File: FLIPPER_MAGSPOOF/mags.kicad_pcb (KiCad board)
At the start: 2 copper layers, 67 x 34 mm, 5 parts, among them J1 Coil, J2 Conn_01x10_Socket, J3 Conn_01x08_Socket, U1 TC4424

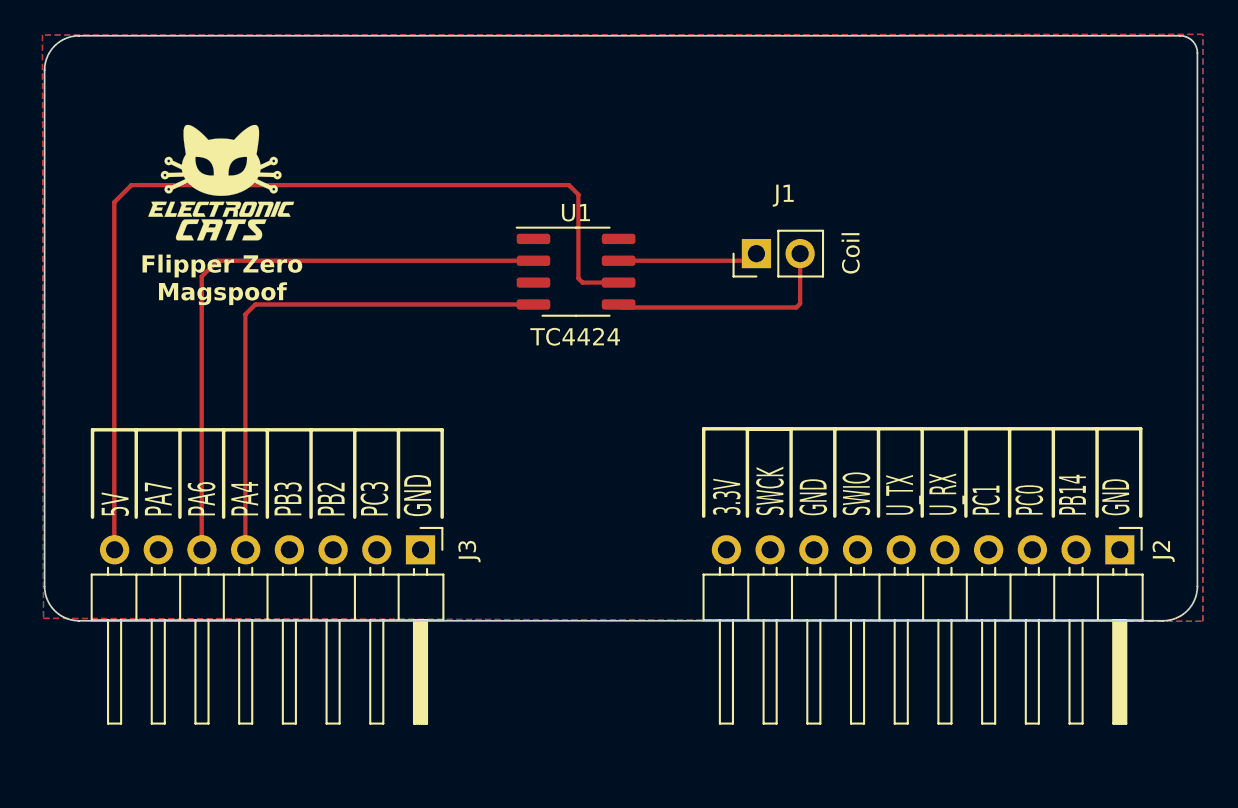
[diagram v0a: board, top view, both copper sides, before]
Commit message: add BOM and serigraphy
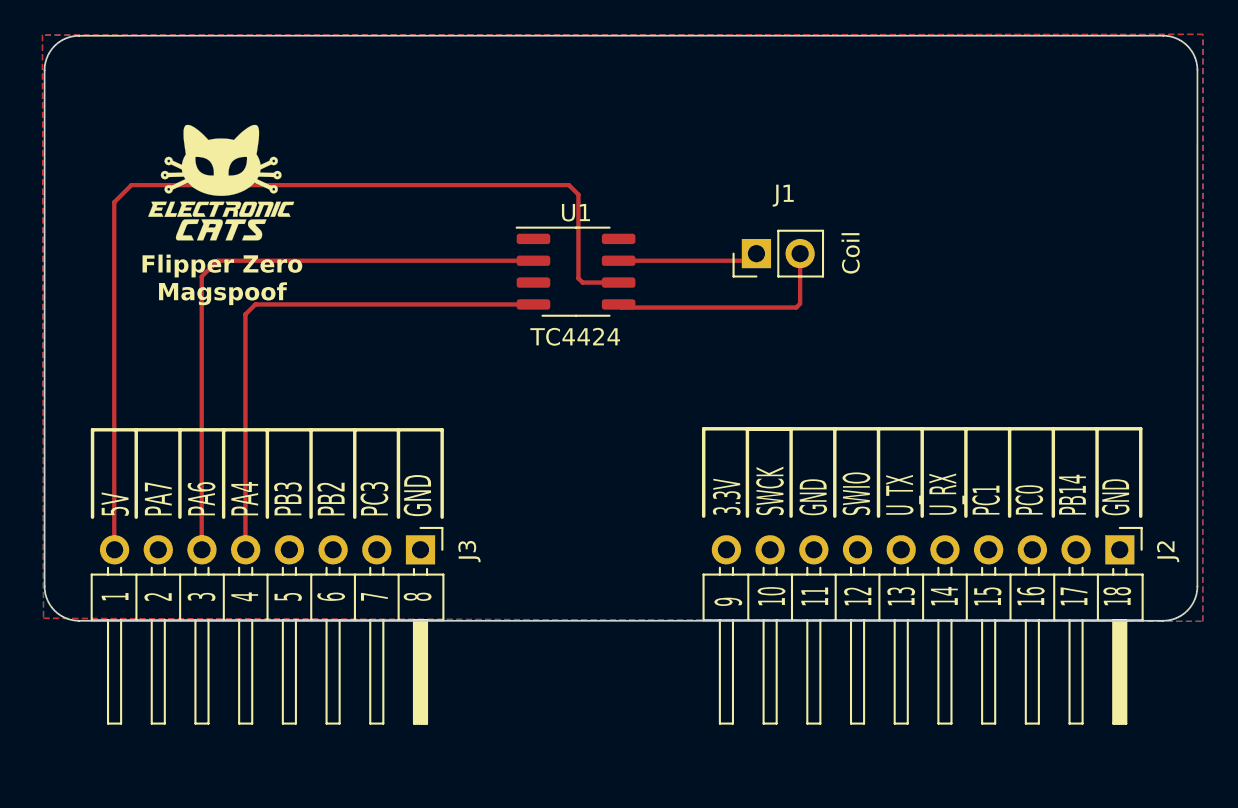
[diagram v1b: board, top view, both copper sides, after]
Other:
- outline, holes or cut-outs redrawn
- board text added: "1 2 3 4 5 6 7 8"
- board text added: "9 10 11 12 13 14 15 16 17 18"
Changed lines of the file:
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@@
         (effects (font (size 1 1) (thickness 0.15)))
     )
-    (fp_text user "${REFERENCE}" (at 2.77 8.89) (layer "F.Fab")
-        (effects (font (size 1 1) (thickness 0.15)))
-    )
     (fp_line (start -1.27 -1.27) (end 0 -1.27)
       (stroke (width 0.12) (type solid)) (layer "F.SilkS"))
@@
       (net 8 "+5V") (pinfunction "Pin_1") (pintype "passive"))
     (model "${KICAD6_3DMODEL_DIR}/Connector_PinHeader_2.54mm.3dshapes/PinHeader_1x08_P2.54mm_Horizontal.wrl"
-      (offset (xyz 0 0 0))
+      (offset (xyz 0 -17.75 -1))
       (scale (xyz 1 1 1))
-      (rotate (xyz 0 0 0))
+      (rotate (xyz 180 0 0))
     )
   )
@@
     (property "ki_keywords" "connector")
     (attr through_hole)
-    (fp_text reference "J2" (at -0.0032 -2.459 90) (layer "F.SilkS")
+    (fp_text reference "J2" (at 0.0068 -2.719 90) (layer "F.SilkS")
         (effects (font (size 1 1) (thickness 0.15)))
     )
@@
       (net 16 "unconnected-(J2-Pin_1-Pad10)") (pinfunction "Pin_1") (pintype "passive+no_connect"))
     (model "${KICAD6_3DMODEL_DIR}/Connector_PinHeader_2.54mm.3dshapes/PinHeader_1x10_P2.54mm_Horizontal.wrl"
-      (offset (xyz 0 0 0))
+      (offset (xyz 0 -22.75 -1))
       (scale (xyz 1 1 1))
-      (rotate (xyz 0 0 0))
+      (rotate (xyz 0 180 180))
     )
   )
@@
   (gr_line (start 244.47 75.49) (end 244.47 80.57)
     (stroke (width 0.2) (type solid)) (layer "F.SilkS"))
-  (gr_line (start 263.0042 53.65) (end 263.0042 84.65)
+  (gr_line (start 263.005786 54.644214) (end 263.0042 84.65)
     (stroke (width 0.1) (type default)) (layer "Edge.Cuts"))
   (gr_line (start 196.0042 84.65) (end 196.0042 54.65)
     (stroke (width 0.1) (type default)) (layer "Edge.Cuts"))
-  (gr_line (start 198.0042 52.65) (end 262.0042 52.65)
+  (gr_line (start 198.0042 52.65) (end 261.005786 52.644214)
     (stroke (width 0.1) (type default)) (layer "Edge.Cuts"))
   (gr_line (start 261.0042 86.65) (end 198.0042 86.65)
     (stroke (width 0.1) (type default)) (layer "Edge.Cuts"))
-  (gr_arc (start 262.0042 52.65) (mid 262.711306 52.942893) (end 263.0042 53.65)
-    (stroke (width 0.1) (type default)) (layer "Edge.Cuts"))
   (gr_arc (start 198.0042 86.65) (mid 196.589986 86.064214) (end 196.0042 84.65)
     (stroke (width 0.1) (type default)) (layer "Edge.Cuts"))
@@
   (gr_arc (start 263.0042 84.65) (mid 262.418414 86.064214) (end 261.0042 86.65)
     (stroke (width 0.1) (type default)) (layer "Edge.Cuts"))
+  (gr_arc (start 261.005786 52.644214) (mid 262.42 53.23) (end 263.005786 54.644214)
+    (stroke (width 0.1) (type default)) (layer "Edge.Cuts"))
+  (gr_text "1\n2\n3\n4\n5\n6\n7\n8" (at 208.95 85.56 90) (layer "F.SilkS")
+    (effects (font (size 1.56 0.7) (thickness 0.175)) (justify left))
+  )
   (gr_text "Flipper Zero\nMagspoof" (at 206.3042 66.75) (layer "F.SilkS")
     (effects (font (size 1 1) (thickness 0.25) bold))
@@
     (effects (font (size 1.56 0.7) (thickness 0.175)) (justify left))
   )
+  (gr_text "9\n10\n11\n12\n13\n14\n15\n16\n17\n18" (at 247.1 85.85 90) (layer "F.SilkS")
+    (effects (font (size 1.56 0.7) (thickness 0.175)) (justify left))
+  )
   (gr_text "5V\nPA7\nPA6\nPA4\nPB3\nPB2\nPC3\nGND" (at 208.95 80.63 90) (layer "F.SilkS")
     (effects (font (size 1.56 0.8) (thickness 0.2)) (justify left))
@@
   )
   (dimension (type aligned) (layer "Margin")
-    (pts (xy 262.7697 57.174) (xy 195.8697 56.874))
-    (height 16.376324)
-    (gr_text "66.9007 mm" (at 257.4197 37.924 -0.2569300245) (layer "Margin")
-      (effects (font (size 1.5 1.5) (thickness 0.3)))
-    )
-    (format (prefix "") (suffix "") (units 3) (units_format 1) (precision 4))
-    (style (thickness 0.2) (arrow_length 1.27) (text_position_mode 2) (extension_height 0.58642) (extension_offset 0.5) keep_text_aligned)
-  )
-  (dimension (type aligned) (layer "Margin")

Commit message: add version "v1.0"
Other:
- board text added: "Flipper Zero Magspoof v1.0"
- board text removed: "Flipper Zero Magspoof"
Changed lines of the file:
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@@
       (outputformat 1)
       (mirror false)
-      (drillshape 1)
+      (drillshape 0)
       (scaleselection 1)
-      (outputdirectory "")
+      (outputdirectory "flipper_magspoof_v1.0_gerbers")
     )
   )
@@
     (effects (font (size 1.56 0.7) (thickness 0.175)) (justify left))
   )
-  (gr_text "Flipper Zero\nMagspoof" (at 206.3042 66.75) (layer "F.SilkS")
+  (gr_text "Flipper Zero\nMagspoof v1.0" (at 206.3042 66.75) (layer "F.SilkS")
     (effects (font (size 1 1) (thickness 0.25) bold))
   )

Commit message: Change_Coil
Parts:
- removed G***: LOGO, Aesthetics:electronic_cats_logo_8x6
- added kibuzzard-6488EE7C: G***, kibuzzard-6488EE7C, F.Cu at (200.1, 78.5)
- added kibuzzard-6488EE8B: G***, kibuzzard-6488EE8B, F.Cu at (202.6, 78.2)
- added kibuzzard-6488EE9B: G***, kibuzzard-6488EE9B, F.Cu at (205.3, 78.3)
- added kibuzzard-6488EEAF: G***, kibuzzard-6488EEAF, F.Cu at (258.5, 78.8)
- added kibuzzard-6488EEAF: G***, kibuzzard-6488EEAF, F.Cu at (218.0, 78.5)
- added kibuzzard-6488EEAF: G***, kibuzzard-6488EEAF, F.Cu at (240.7, 78.9)
- moved J1 25.3 mm to (212.1, 65.2)
- moved U1 16.0 mm to (212.7, 73.8), turned to 90 degrees
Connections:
- J3 pad 5: /IN_B -> unconnected-(J3-Pin_4-Pad5)
- J3 pad 6: /IN_A -> /IN_B
- J3 pad 7: unconnected-(J3-Pin_2-Pad7) -> /IN_A
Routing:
- net +5V: track 55.1 -> 23.8 mm
- net /IN_A: track 35.5 -> 14.9 mm
- net /IN_B: track 30.7 -> 15.2 mm
- net /Out_B: track 13.6 -> 6.13 mm
- net /Out_A: track 8.18 -> 6.13 mm
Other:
- board size 67 x 34 mm -> 67 x 23.3 mm
- board text removed: "1 2 3 4 5 6 7 8"
- board text removed: "3.3V SWCK GND SWIO U_TX U_RX PC1 PC0 PB14 GND"
- board text removed: "5V PA7 PA6 PA4 PB3 PB2 PC3 GND"
- board text removed: "9 10 11 12 13 14 15 16 17 18"

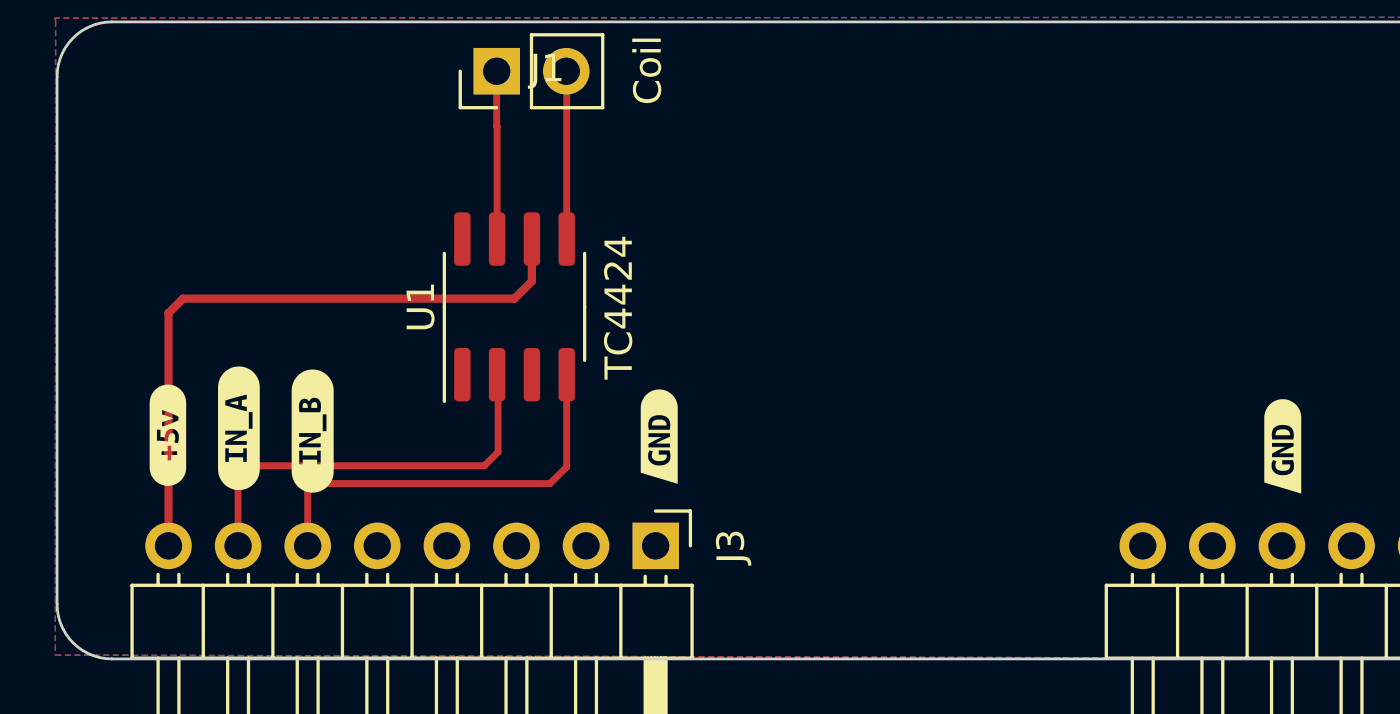
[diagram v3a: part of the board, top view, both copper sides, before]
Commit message: Add_Boost
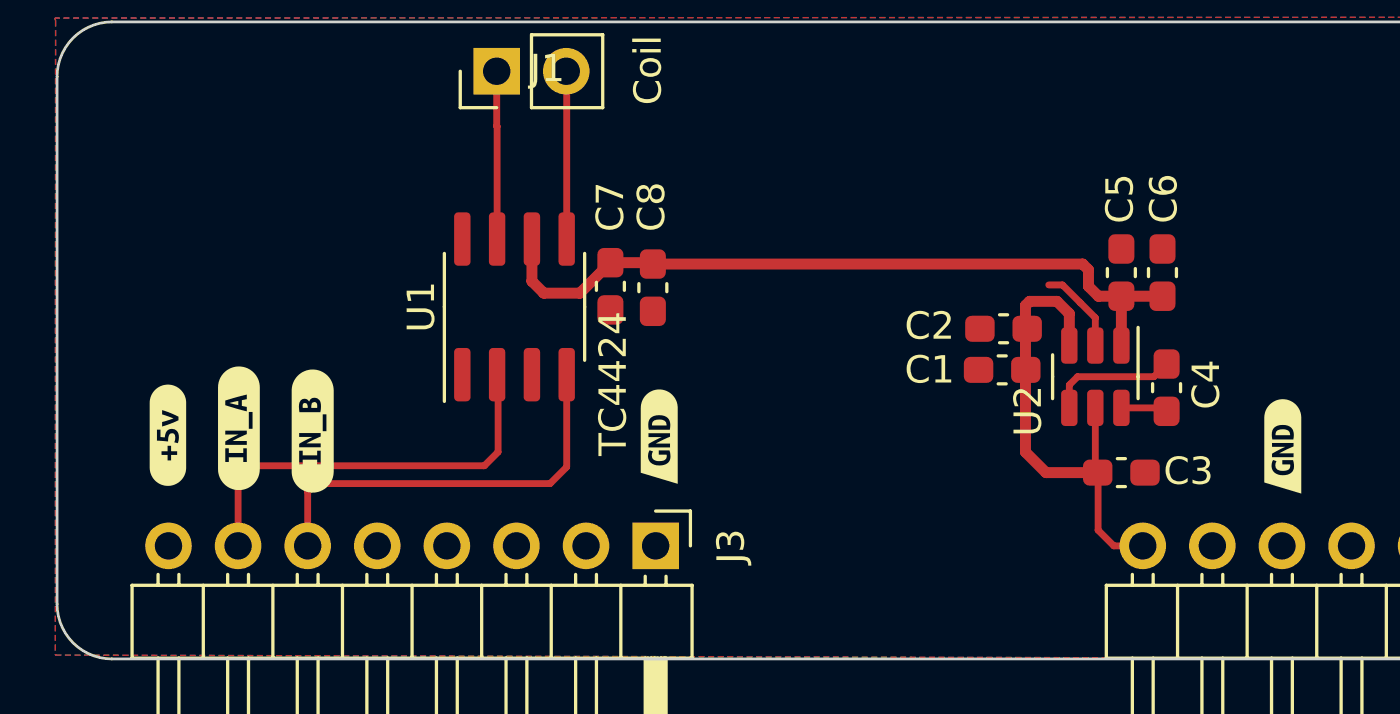
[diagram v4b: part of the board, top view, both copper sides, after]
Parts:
- added C1: 0.1uf, Capacitor_SMD:C_0603_1608Metric_Pad1.08x0.95mm_HandSolder, F.Cu at (230.5, 76.1)
- added C2: 10uf, Capacitor_SMD:C_0603_1608Metric_Pad1.08x0.95mm_HandSolder, F.Cu at (230.6, 74.6)
- added C3: 10uf, Capacitor_SMD:C_0603_1608Metric_Pad1.08x0.95mm_HandSolder, F.Cu at (234.8, 79.8)
- added C4: 1uf, Capacitor_SMD:C_0603_1608Metric_Pad1.08x0.95mm_HandSolder, F.Cu at (236.5, 76.8)
- added C5: 10uf, Capacitor_SMD:C_0603_1608Metric_Pad1.08x0.95mm_HandSolder, F.Cu at (234.8, 72.5)
- added C6: 0.1uf, Capacitor_SMD:C_0603_1608Metric_Pad1.08x0.95mm_HandSolder, F.Cu at (236.3, 72.5)
- added C7: 10uf, Capacitor_SMD:C_0603_1608Metric_Pad1.08x0.95mm_HandSolder, F.Cu at (216.2, 73.0)
- added C8: 0.1uf, Capacitor_SMD:C_0603_1608Metric_Pad1.08x0.95mm_HandSolder, F.Cu at (217.8, 73.1)
- added U2: AP3602AKTR-G1, Package_TO_SOT_SMD:TSOT-23-6, F.Cu at (233.9, 76.3)
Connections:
- J2 pad 10: unconnected-(J2-Pin_1-Pad10) -> +3V3
- J3 pad 8: +5V -> unconnected-(J3-Pin_1-Pad8)
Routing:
- net +3V3: track 0.00 -> 17.7 mm
- net Net-(U2-C-): track 0.00 -> 4.70 mm
- net +5V: track 23.8 -> 27.9 mm
- net GND: track 0.00 -> 3.21 mm
- net Net-(U2-C+): track 0.00 -> 1.70 mm

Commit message: Add_Labels
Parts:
- removed kibuzzard-6488EE7C: G***, kibuzzard-6488EE7C
- removed kibuzzard-6488EE8B: G***, kibuzzard-6488EE8B
- removed kibuzzard-6488EE9B: G***, kibuzzard-6488EE9B
- added kibuzzard-6488F75A: G***, kibuzzard-6488F75A, F.Cu at (235.7, 79.9)
- added kibuzzard-6488F7DC: G***, kibuzzard-6488F7DC, F.Cu at (202.4, 80.0)
- added kibuzzard-6488F7EB: G***, kibuzzard-6488F7EB, F.Cu at (205.2, 80.0)
- moved C3 3.76 mm to (231.1, 79.7), turned to 180 degrees
- moved kibuzzard-6488EEAF 1.36 mm to (218.0, 79.9), turned to 0 degrees
- moved kibuzzard-6488EEAF 1.06 mm to (258.5, 79.9), turned to 0 degrees
- moved kibuzzard-6488EEAF 1.01 mm to (240.8, 79.9), turned to 0 degrees
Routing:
- net +3V3: track 17.7 -> 19.2 mm

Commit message: add logo EC
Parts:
- added G***: LOGO, Symbol_EC:electronic_cats_logo_8x6, F.Cu at (251.8, 74.4)
- added G***: LOGO, Symbol_EC:electronic_cats_logo_8x6, B.Cu at (251.8, 74.4)
- added REF**: OSHW-Logo2_9.8x8mm_SilkScreen, Symbol:OSHW-Logo2_9.8x8mm_SilkScreen, F.Cu at (203.5, 74.4)
- added REF**: OSHW-Logo2_9.8x8mm_SilkScreen, Symbol:OSHW-Logo2_9.8x8mm_SilkScreen, B.Cu at (203.5, 74.4)
- moved kibuzzard-6488EEAF 0.96 mm to (258.5, 78.9), turned to 90 degrees
- moved kibuzzard-6488EEAF 0.78 mm to (218.0, 79.1), turned to 90 degrees
- moved kibuzzard-6488EEAF 0.78 mm to (240.5, 79.2), turned to 90 degrees
- turned kibuzzard-6488F7DC to 90 degrees
- turned kibuzzard-6488F7EB to 90 degrees
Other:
- board text added: "Backpack Magspoof Flipper Zero v1.0"
- board text removed: "Flipper Zero Magspoof v1.0"
